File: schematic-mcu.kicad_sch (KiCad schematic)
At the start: 22 parts, among them U5 USBLC6-2P6, U6 ESP32-S3FN8, Y1 Crystal_GND24

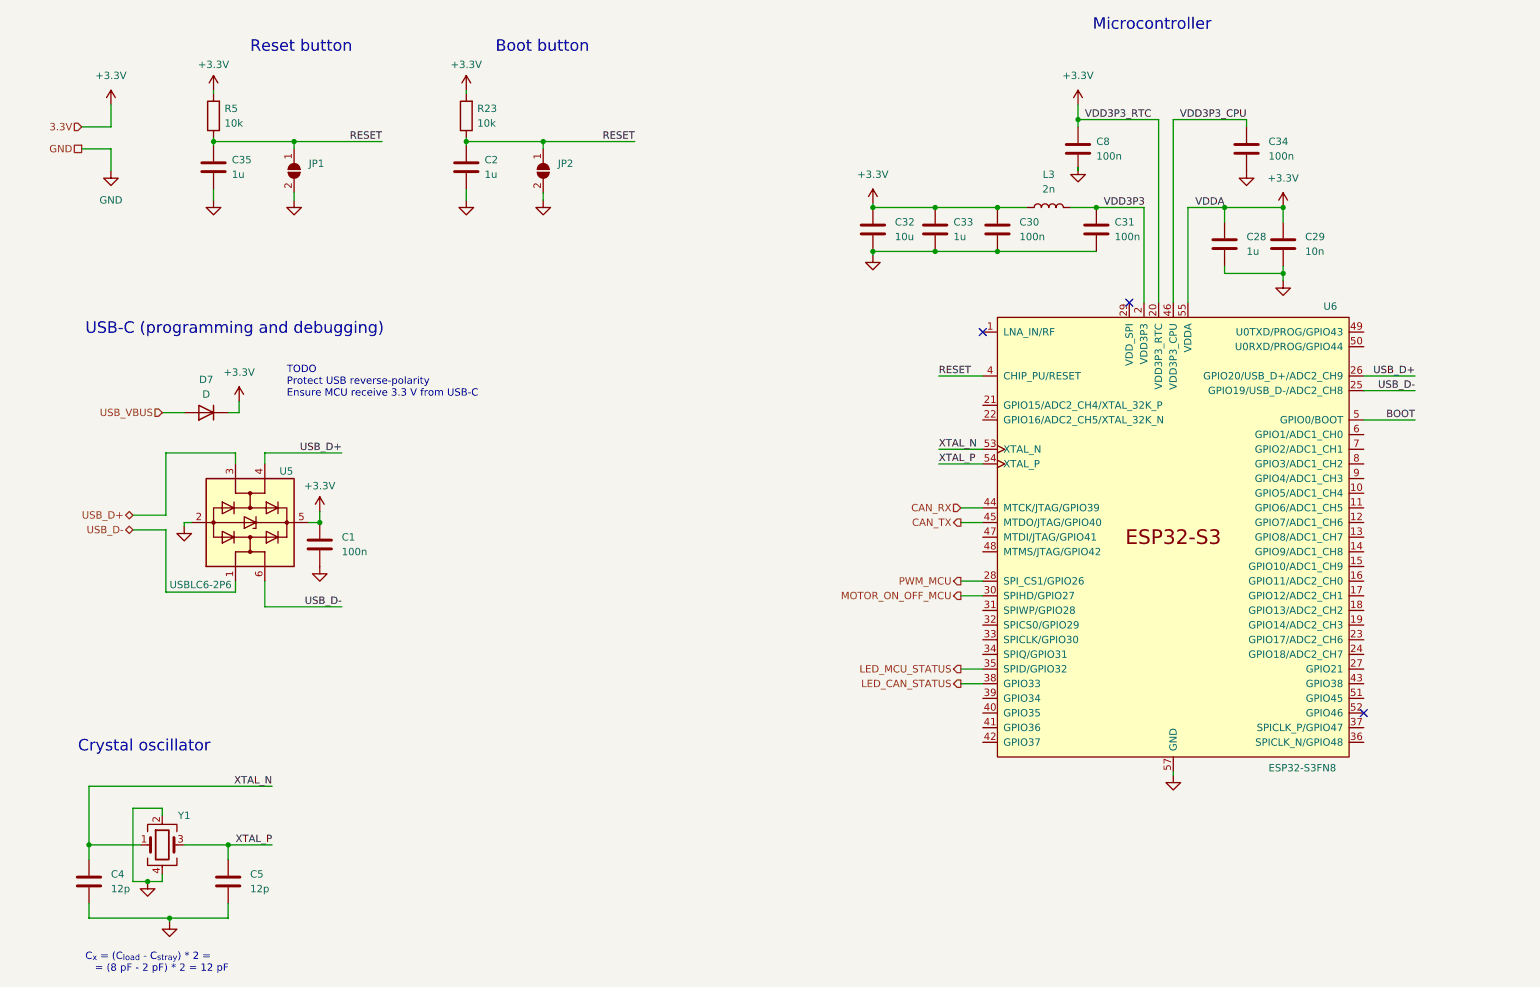
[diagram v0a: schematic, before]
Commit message: Fix most issues with found after ERC
Grid size, unconnected ping, PWR_FLAGs
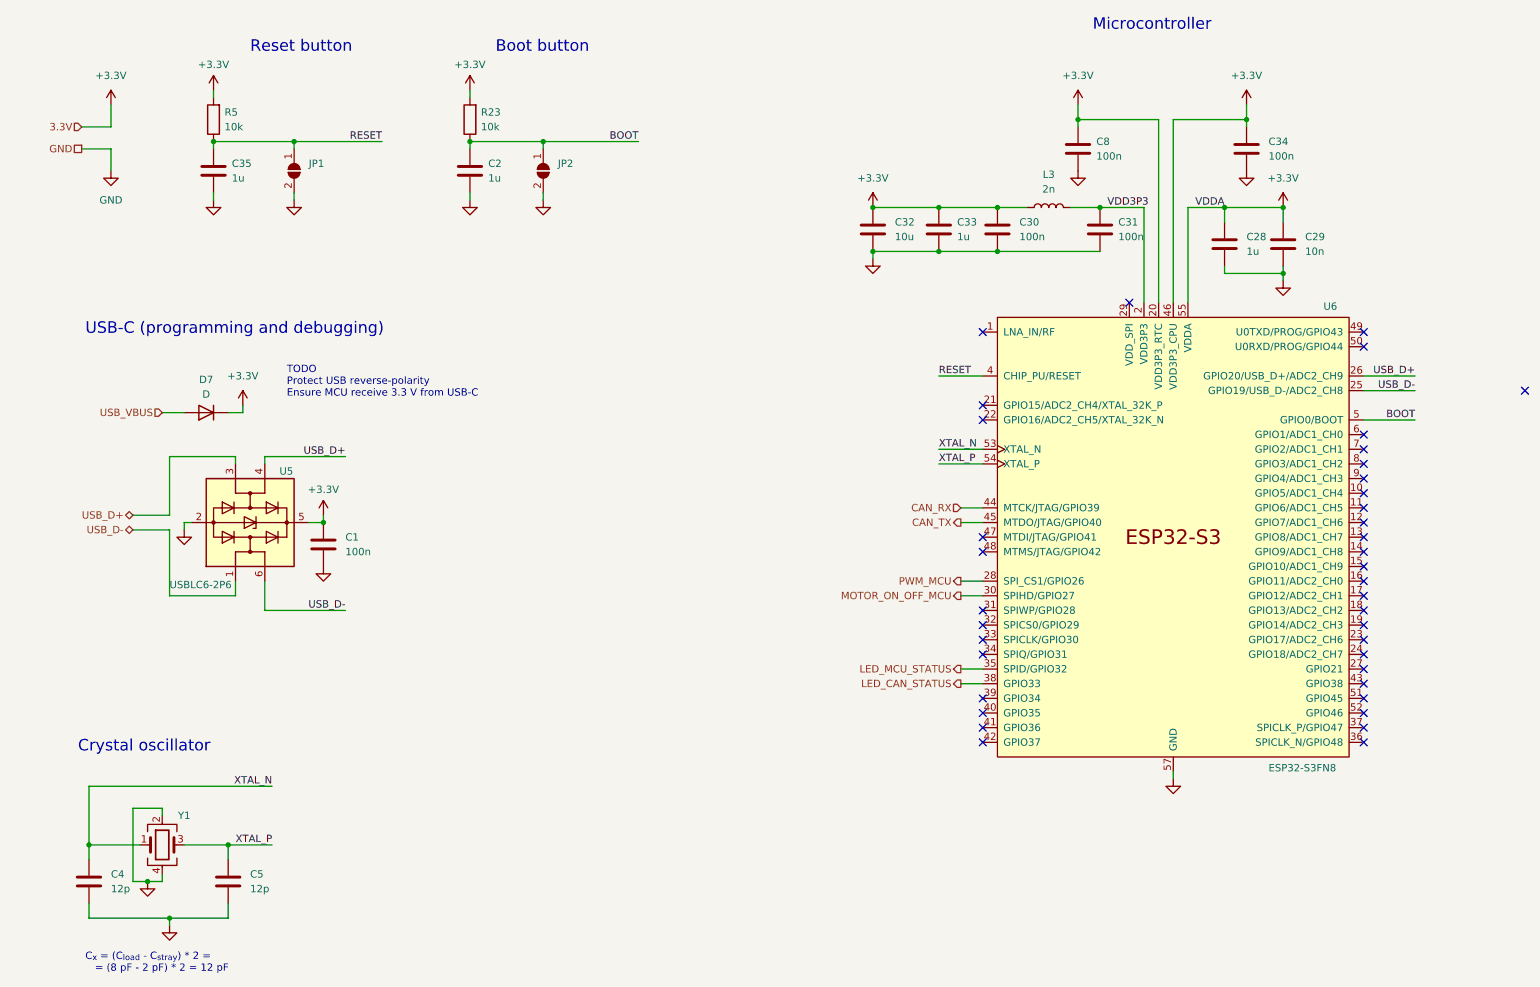
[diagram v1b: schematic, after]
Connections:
- net VDD3P3_CPU is gone; now on net +3.3V: C34.1, U6.46 (VDD3P3_CPU)
- net BOOT: now also C2.1, JP2.1 (A), R23.1
- net RESET: no longer C2.1, JP2.1 (A), R23.1
- no-connect marks 3 -> 39
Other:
- company: (none) -> Hydrogreen Pollub
- title: (none) -> Motor driver unit
- moved on the sheet: C1, C2, C31, C33, C35, R23, R5

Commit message: Add test MCU pad
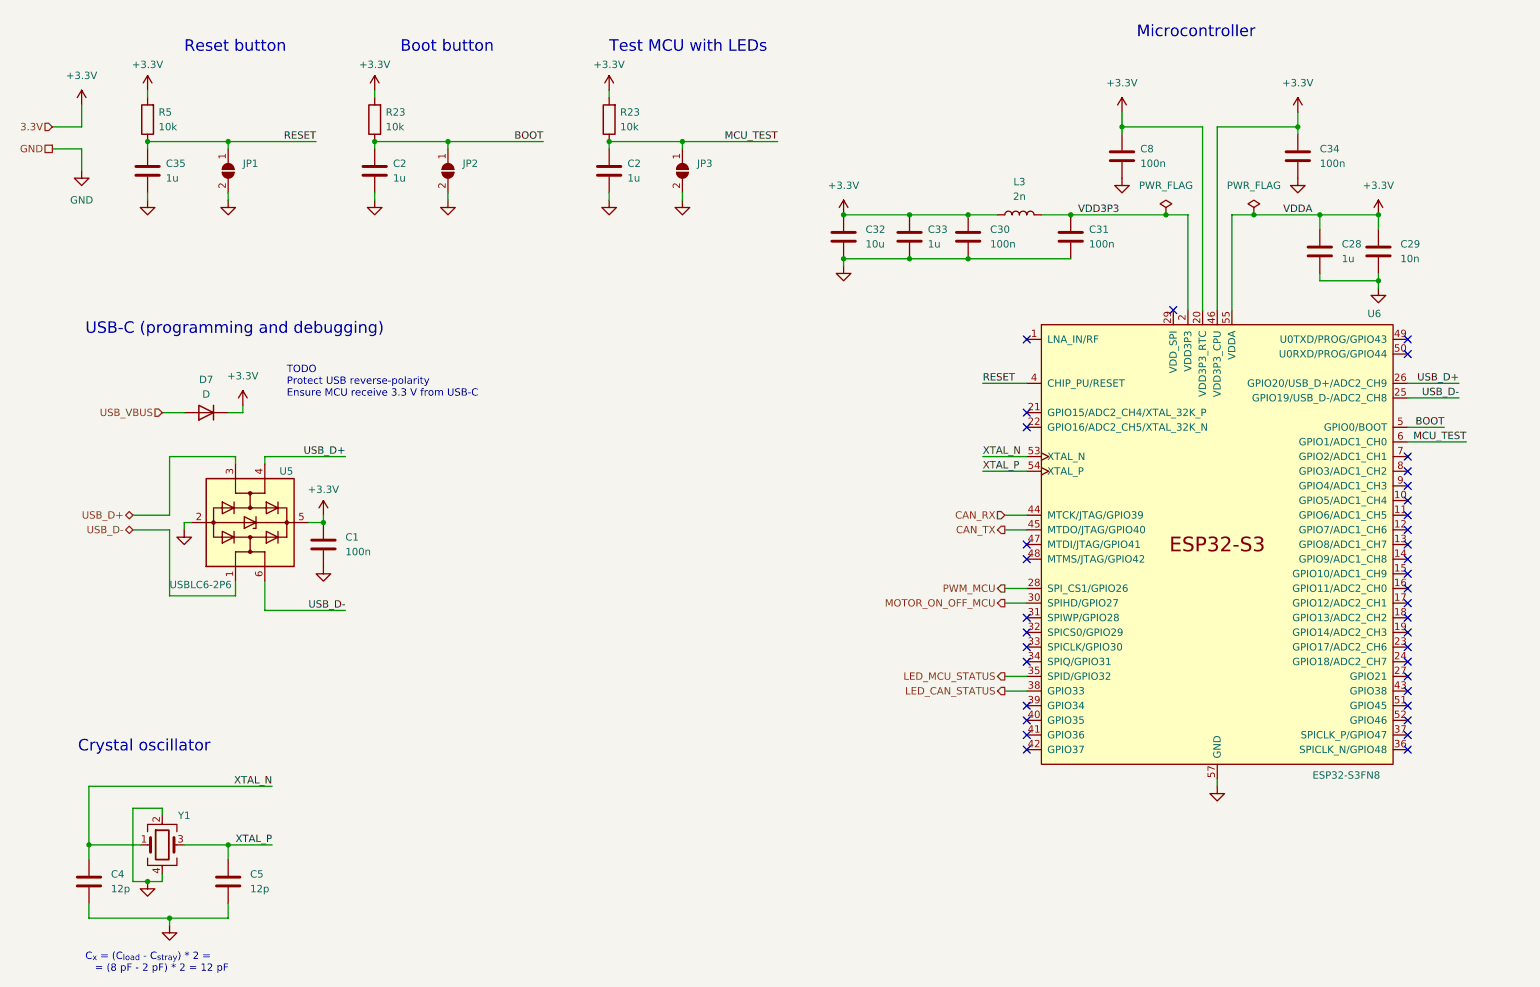
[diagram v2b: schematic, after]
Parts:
- added C2: 1u, symbol Device:C
- added JP3: SolderJumper_2_Open, Jumper:SolderJumper-2_P1.3mm_Open_Pad1.0x1.5mm, symbol Jumper:SolderJumper_2_Open
- added R23: 10k, symbol Device:R
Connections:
- net +3.3V: now also R23.2
- net GND: now also C2.2, JP3.2 (B)
- net MCU_TEST: now reaches U6.6 (GPIO1/ADC1_CH0)
- net MCU_TEST: now also C2.1, JP3.1 (A), R23.1
- no-connect marks 39 -> 37
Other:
- note added: "Test MCU with LEDs"
- moved on the sheet: C2, C28, C29, C30, C31, C32, C33, C34, C35, C8, JP1, JP2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

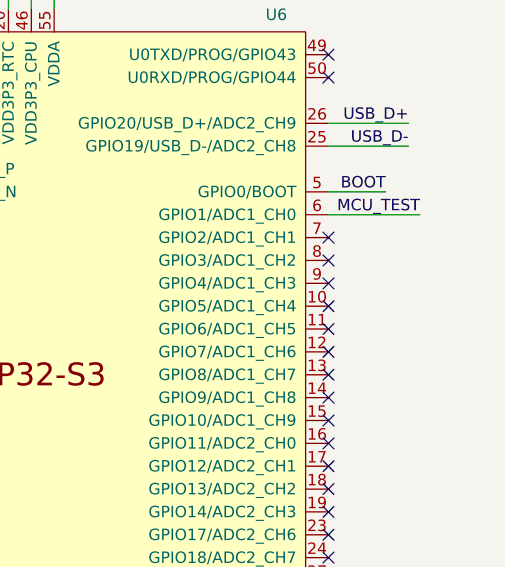
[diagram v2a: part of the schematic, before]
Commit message: Add values for ideal diode circuit
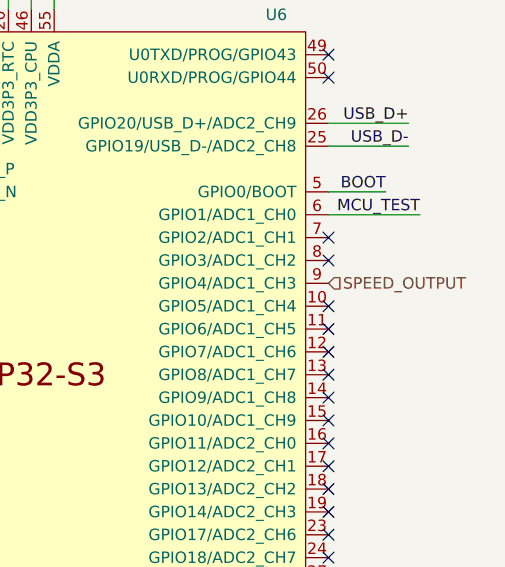
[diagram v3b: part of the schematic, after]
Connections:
- net SPEED_OUTPUT: now reaches U6.9 (GPIO4/ADC1_CH3)
- no-connect marks 37 -> 36
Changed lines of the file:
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@@
   (no_connect (at 261.62 97.79))
   (no_connect (at 261.62 128.27))
-  (no_connect (at 261.62 100.33))
   (no_connect (at 261.62 123.19))
   (no_connect (at 261.62 133.35))
@@
     (effects (font (size 1.27 1.27)) (justify right))
   )
+  (hierarchical_label "SPEED_OUTPUT" (shape input) (at 261.62 100.33 0) (fields_autoplaced)
+    (effects (font (size 1.27 1.27)) (justify left))
+  )
   (hierarchical_label "MOTOR_ON_OFF_MCU" (shape output) (at 191.77 120.65 180) (fields_autoplaced)

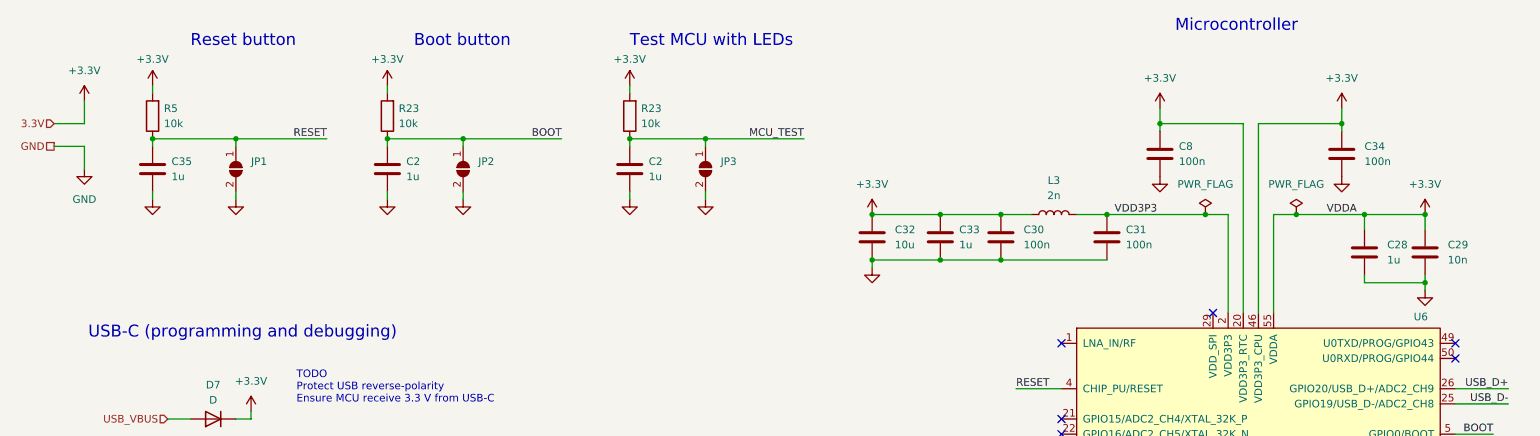
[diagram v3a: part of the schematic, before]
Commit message: Fix ERC checks related to hierarchical labels
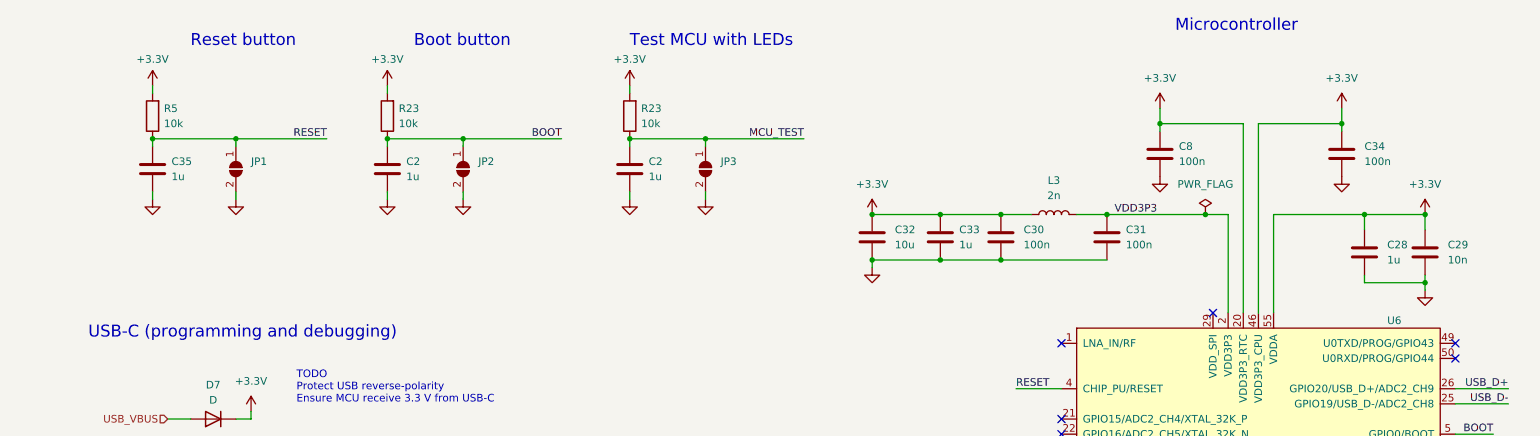
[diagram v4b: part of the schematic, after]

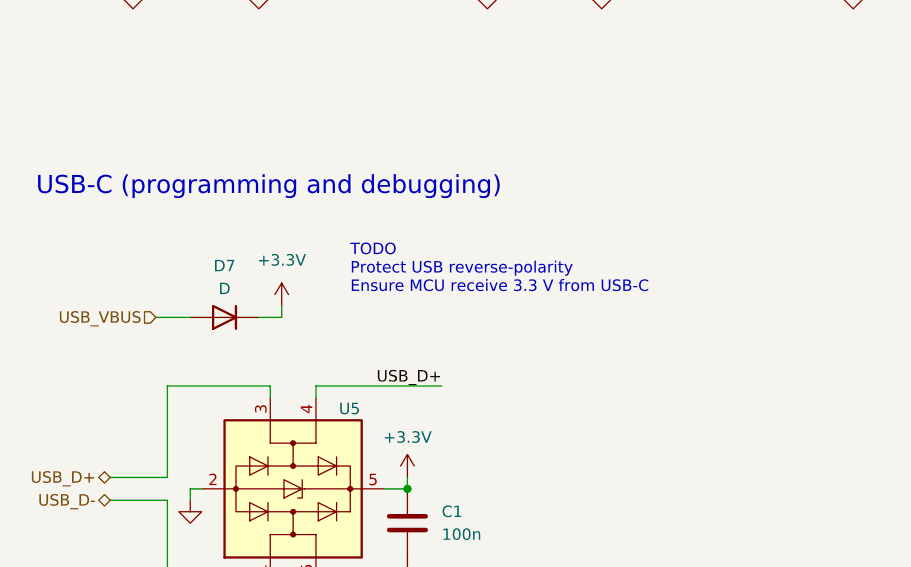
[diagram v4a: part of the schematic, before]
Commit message: Add Schottky Diode for VBUS and Vreg
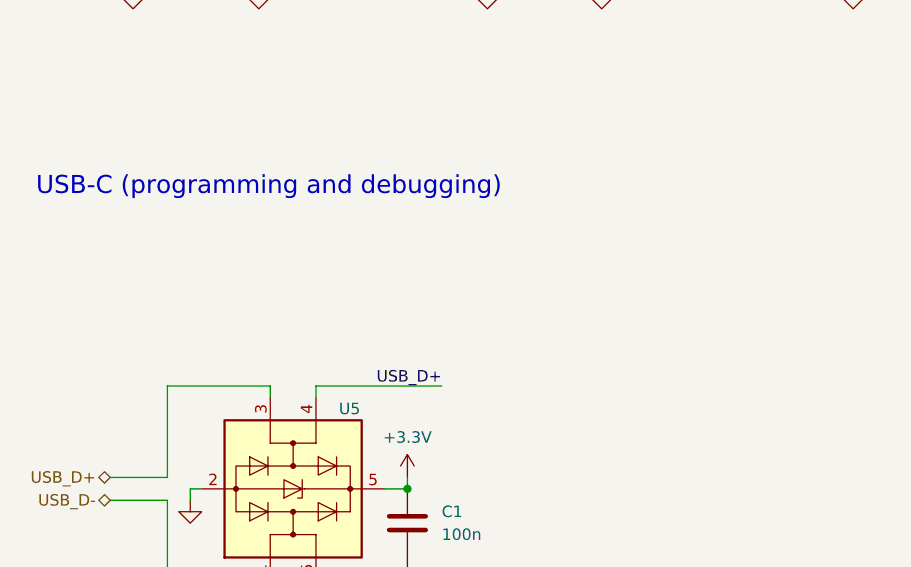
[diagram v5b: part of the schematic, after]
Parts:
- removed D7: D, symbol Device:D
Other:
- note removed: "TODO Protect USB reverse-polarity Ensure MCU receive 3.3 V from USB-C"
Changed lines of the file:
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@@
-    (stroke (width 0) (type default))
-  )
-  (wire (pts (xy 59.69 87.63) (xy 59.69 86.36))
     (stroke (width 0) (type default))
   )
@@
     (stroke (width 0) (type default))
   )
-  (wire (pts (xy 45.72 87.63) (xy 49.53 87.63))
-    (stroke (width 0) (type default))
-  )
   (wire (pts (xy 191.77 135.89) (xy 195.58 135.89))
     (stroke (width 0) (type default))
@@
   )
   (wire (pts (xy 270.51 85.09) (xy 261.62 85.09))
-    (stroke (width 0) (type default))
-  )
-  (wire (pts (xy 57.15 87.63) (xy 59.69 87.63))
     (stroke (width 0) (type default))
   )
@@
   (text "Microcontroller" (at 214.63 22.86 0)
     (effects (font (size 2 2)) (justify left bottom))
-  )
-  (text "TODO\nProtect USB reverse-polarity\nEnsure MCU receive 3.3 V from USB-C\n"
-    (at 67.31 85.09 0)
-    (effects (font (size 1.27 1.27)) (justify left bottom))
   )
   (text "Reset button" (at 49.53 25.4 0)
@@
   )
   (hierarchical_label "PWM_MCU" (shape output) (at 191.77 118.11 180) (fields_autoplaced)
-    (effects (font (size 1.27 1.27)) (justify right))
-  )
-  (hierarchical_label "USB_VBUS" (shape input) (at 45.72 87.63 180) (fields_autoplaced)
     (effects (font (size 1.27 1.27)) (justify right))
   )
@@
     )
   )
-  (symbol (lib_id "power:+3.3V") (at 59.69 86.36 0) (unit 1)
-    (in_bom yes) (on_board yes) (dnp no) (fields_autoplaced)
-    (property "Reference" "#PWR036" (at 59.69 90.17 0)
-      (effects (font (size 1.27 1.27)) hide)
-    )
-    (property "Value" "+3.3V" (at 59.69 81.28 0)
-      (effects (font (size 1.27 1.27)))
-    )
-    (property "Footprint" "" (at 59.69 86.36 0)
-      (effects (font (size 1.27 1.27)) hide)
-    )
-    (property "Datasheet" "" (at 59.69 86.36 0)
-      (effects (font (size 1.27 1.27)) hide)
-    )
-    (pin "1")
-    (instances
-      (project "schematic-main"
-        (path "/c9ad7189-d3b2-414a-9743-efd8e57cd755"
-          (reference "#PWR036") (unit 1)
-        )
-        (path "/c9ad7189-d3b2-414a-9743-efd8e57cd755/f92f58ec-64e0-437c-bc00-8ae46a3b3054"
-          (reference "#PWR031") (unit 1)
-        )
-      )
-    )
-  )
   (symbol (lib_id "power:GND") (at 73.66 114.3 0) (unit 1)
     (in_bom yes) (on_board yes) (dnp no) (fields_autoplaced)
@@
         )
       )
-    )
-  )
-  (symbol (lib_id "Device:D") (at 53.34 87.63 180) (unit 1)
-    (in_bom yes) (on_board yes) (dnp no) (fields_autoplaced)
-    (property "Reference" "D7" (at 53.34 81.915 0)
-      (effects (font (size 1.27 1.27)))
-    )
-    (property "Value" "D" (at 53.34 84.455 0)
-      (effects (font (size 1.27 1.27)))
-    )
-    (property "Footprint" "" (at 53.34 87.63 0)
-      (effects (font (size 1.27 1.27)) hide)
-    )
-    (property "Datasheet" "~" (at 53.34 87.63 0)
-      (effects (font (size 1.27 1.27)) hide)
-    )
-    (property "Sim.Device" "D" (at 53.34 87.63 0)
-      (effects (font (size 1.27 1.27)) hide)
-    )
-    (property "Sim.Pins" "1=K 2=A" (at 53.34 87.63 0)
-      (effects (font (size 1.27 1.27)) hide)
-    )
-    (pin "1")
-    (pin "2")
-    (instances
-      (project "schematic-main"
-        (path "/c9ad7189-d3b2-414a-9743-efd8e57cd755"
-          (reference "D7") (unit 1)
-        )
-        (path "/c9ad7189-d3b2-414a-9743-efd8e57cd755/f92f58ec-64e0-437c-bc00-8ae46a3b3054"
-          (reference "D2") (unit 1)
-        )
-      )
